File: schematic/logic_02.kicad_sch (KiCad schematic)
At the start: 4 parts, among them U405 74HC04, U408 74HC04, U416 74HC04, U420 74HC04

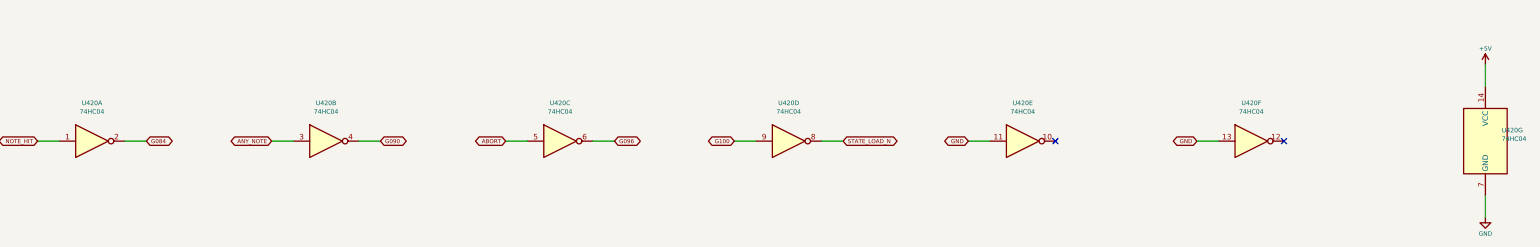
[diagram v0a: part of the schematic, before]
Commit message: add power supply, rail checks and parts list
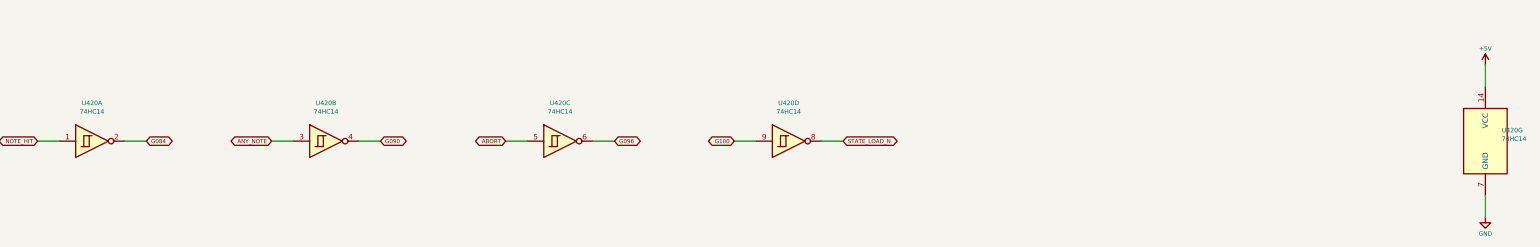
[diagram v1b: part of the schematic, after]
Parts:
- removed unit 6 of U420
- removed unit 5 of U420
- U405, U408, U416: MPN (none) -> 74HC04D,653; Manufacturer (none) -> Nexperia; Supplier (none) -> LCSC
- U420: value 74HC04 -> 74HC14; symbol 74xx:74HC04 -> 74xx:74HC14; MPN (none) -> 74HC14D,653; Manufacturer (none) -> Nexperia; Supplier (none) -> LCSC
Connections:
- no-connect marks 2 -> 0
